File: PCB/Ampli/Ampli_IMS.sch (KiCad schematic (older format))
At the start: 22 parts, among them J1 5227161-3, J2 5227161-3, J3 Conn_01x03_Male, SW1 SS22D0205G2, U1 LT1464CS8, U2 LMP7721

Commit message: modif of schematics
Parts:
- removed U2: LMP7721, Package_SO:SOIC-8_3.9x4.9mm_P1.27mm, symbol Ampli_IMS-rescue:AD8001AR-Amplifier_Operational
- added U?: ADA4625-1, Package_DIP:DIP-8_W7.62mm, symbol Amplifier_Operational:ADA4625-1
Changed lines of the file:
@@
-$EndComp
-$Comp
-L Ampli_IMS-rescue:AD8001AR-Amplifier_Operational U2
-U 1 1 5E63EDD1
-P 4200 4250
-F 0 "U2" H 4544 4296 50  0000 L CNN
-F 1 "LMP7721" H 4544 4205 50  0000 L CNN
-F 2 "Package_SO:SOIC-8_3.9x4.9mm_P1.27mm" H 4100 4050 50  0001 L CNN
-F 3 "https://www.analog.com/media/en/technical-documentation/data-sheets/ad8001.pdf" H 4350 4400 50  0001 C CNN
-	1    4200 4250
-	1    0    0    -1
 $EndComp
 $Comp
@@
 Text Notes 3550 5100 0    50   ~ 0
 Capacités de découplage\n
+$Comp
+L Amplifier_Operational:ADA4625-1 U?
+U 1 1 5E61DA9C
+P 4200 4250
+F 0 "U?" H 4544 4296 50  0000 L CNN
+F 1 "ADA4625-1" H 4544 4205 50  0000 L CNN
+F 2 "Package_DIP:DIP-8_W7.62mm" H 4100 4050 50  0001 L CNN
+F 3 "http://ww1.microchip.com/downloads/en/DeviceDoc/21314g.pdf" H 4350 4400 50  0001 C CNN
+	1    4200 4250
+	1    0    0    -1
+$EndComp
 $EndSCHEMATC

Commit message: tracks realised
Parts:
- U1: renamed from U?; footprint Package_DIP:DIP-8_W7.62mm -> Package_SO:SO-8_3.9x4.9mm_P1.27mm
- U2: renamed from U1; footprint Package_SO:SOIC-8_3.9x4.9mm_P1.27mm -> Package_SO:SO-8_3.9x4.9mm_P1.27mm
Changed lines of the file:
@@
 -15V
 $Comp
-L Ampli_IMS-rescue:Opamp_Dual_Generic-Device U1
+L Ampli_IMS-rescue:Opamp_Dual_Generic-Device U2
 U 1 1 5E681D04
 P 6750 2950
-F 0 "U1" H 6750 3317 50  0000 C CNN
+F 0 "U2" H 6750 3317 50  0000 C CNN
 F 1 "LT1464CS8" H 6750 3226 50  0000 C CNN
-F 2 "Package_SO:SOIC-8_3.9x4.9mm_P1.27mm" H 6750 2950 50  0001 C CNN
+F 2 "Package_SO:SO-8_3.9x4.9mm_P1.27mm" H 6750 2950 50  0001 C CNN
 F 3 "~" H 6750 2950 50  0001 C CNN
 	1    6750 2950
@@
 $EndComp
 $Comp
-L Ampli_IMS-rescue:Opamp_Dual_Generic-Device U1
+L Ampli_IMS-rescue:Opamp_Dual_Generic-Device U2
 U 2 1 5E6829BD
 P 6800 5050
-F 0 "U1" H 6800 5417 50  0000 C CNN
+F 0 "U2" H 6800 5417 50  0000 C CNN
 F 1 "LT1464CS8" H 6800 5326 50  0000 C CNN
-F 2 "Package_SO:SOIC-8_3.9x4.9mm_P1.27mm" H 6800 5050 50  0001 C CNN
+F 2 "Package_SO:SO-8_3.9x4.9mm_P1.27mm" H 6800 5050 50  0001 C CNN
 F 3 "~" H 6800 5050 50  0001 C CNN
 	2    6800 5050
@@
 $EndComp
 $Comp
-L Ampli_IMS-rescue:Opamp_Dual_Generic-Device U1
+L Ampli_IMS-rescue:Opamp_Dual_Generic-Device U2
 U 3 1 5E68341E
 P 1750 6800
-F 0 "U1" H 1708 6846 50  0000 L CNN
+F 0 "U2" H 1708 6846 50  0000 L CNN
 F 1 "LT1464CS8" H 1708 6755 50  0000 L CNN
-F 2 "Package_SO:SOIC-8_3.9x4.9mm_P1.27mm" H 1750 6800 50  0001 C CNN
+F 2 "Package_SO:SO-8_3.9x4.9mm_P1.27mm" H 1750 6800 50  0001 C CNN
 F 3 "~" H 1750 6800 50  0001 C CNN
 	3    1750 6800
@@
 Capacités de découplage\n
 $Comp
-L Amplifier_Operational:ADA4625-1 U?
+L Amplifier_Operational:ADA4625-1 U1
 U 1 1 5E61DA9C
 P 4200 4250
-F 0 "U?" H 4544 4296 50  0000 L CNN
+F 0 "U1" H 4544 4296 50  0000 L CNN
 F 1 "ADA4625-1" H 4544 4205 50  0000 L CNN
-F 2 "Package_DIP:DIP-8_W7.62mm" H 4100 4050 50  0001 L CNN
+F 2 "Package_SO:SO-8_3.9x4.9mm_P1.27mm" H 4100 4050 50  0001 L CNN
 F 3 "http://ww1.microchip.com/downloads/en/DeviceDoc/21314g.pdf" H 4350 4400 50  0001 C CNN
 	1    4200 4250

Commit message: Low noise smd amp
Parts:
- removed R2: 10K MF 1/4W, Resistor_THT:R_Axial_DIN0204_L3.6mm_D1.6mm_P5.08mm_Horizontal, symbol Ampli_IMS-rescue:R-Device
- removed R7: 6.65K MF 1/2W, Resistor_THT:R_Axial_DIN0204_L3.6mm_D1.6mm_P5.08mm_Horizontal, symbol Ampli_IMS-rescue:R-Device
- removed U1: ADA4625-1, Package_SO:SO-8_3.9x4.9mm_P1.27mm, symbol Amplifier_Operational:ADA4625-1
- added U1: LMC6081, Package_SO:SO-8_3.9x4.9mm_P1.27mm, symbol Amplifier_Operational:LMC6081
- C3: renamed from C2; footprint Capacitor_THT:C_Disc_D3.8mm_W2.6mm_P2.50mm -> Capacitor_SMD:C_0805_2012Metric
- C4: renamed from C6; footprint Capacitor_THT:C_Disc_D3.8mm_W2.6mm_P2.50mm -> Capacitor_SMD:C_0805_2012Metric
- C5: renamed from C3; footprint Capacitor_THT:C_Disc_D3.8mm_W2.6mm_P2.50mm -> Capacitor_SMD:C_0805_2012Metric
- C6: renamed from C7; footprint Capacitor_THT:C_Disc_D3.8mm_W2.6mm_P2.50mm -> Capacitor_SMD:C_0805_2012Metric
- C7: renamed from C5; value C_Small -> 100pF; footprint Capacitor_THT:C_Disc_D3.8mm_W2.6mm_P2.50mm -> Capacitor_SMD:C_0805_2012Metric
- J2: renamed from J1; footprint Connector_Coaxial:BNC_Amphenol_B6252HB-NPP3G-50_Horizontal -> Connector_Coaxial:SMA_Amphenol_132203-12_Horizontal
- R1: renamed from R3; footprint Resistor_THT:R_Axial_DIN0204_L3.6mm_D1.6mm_P5.08mm_Horizontal -> Capacitor_SMD:C_0805_2012Metric
- R2: renamed from R1; footprint Resistor_THT:R_Axial_DIN0204_L3.6mm_D1.6mm_P5.08mm_Horizontal -> Capacitor_SMD:C_0805_2012Metric
- R3: renamed from R4; footprint Resistor_THT:R_Axial_DIN0204_L3.6mm_D1.6mm_P5.08mm_Horizontal -> Capacitor_SMD:C_0805_2012Metric
- R4: renamed from R6; value 1.13K MF 1/4W -> 1K; footprint Resistor_THT:R_Axial_DIN0204_L3.6mm_D1.6mm_P5.08mm_Horizontal -> Capacitor_SMD:C_0805_2012Metric
- R5: footprint Resistor_THT:R_Axial_DIN0204_L3.6mm_D1.6mm_P5.08mm_Horizontal -> Capacitor_SMD:C_0805_2012Metric
- renumbered C4 to C2, J3 to J1, J2 to J3
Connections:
- net labels added: +5V, -5V
- net labels removed: +15V, -15V
- wire segments 80 -> 75
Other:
- moved on the sheet: C7, J2, R1, R4

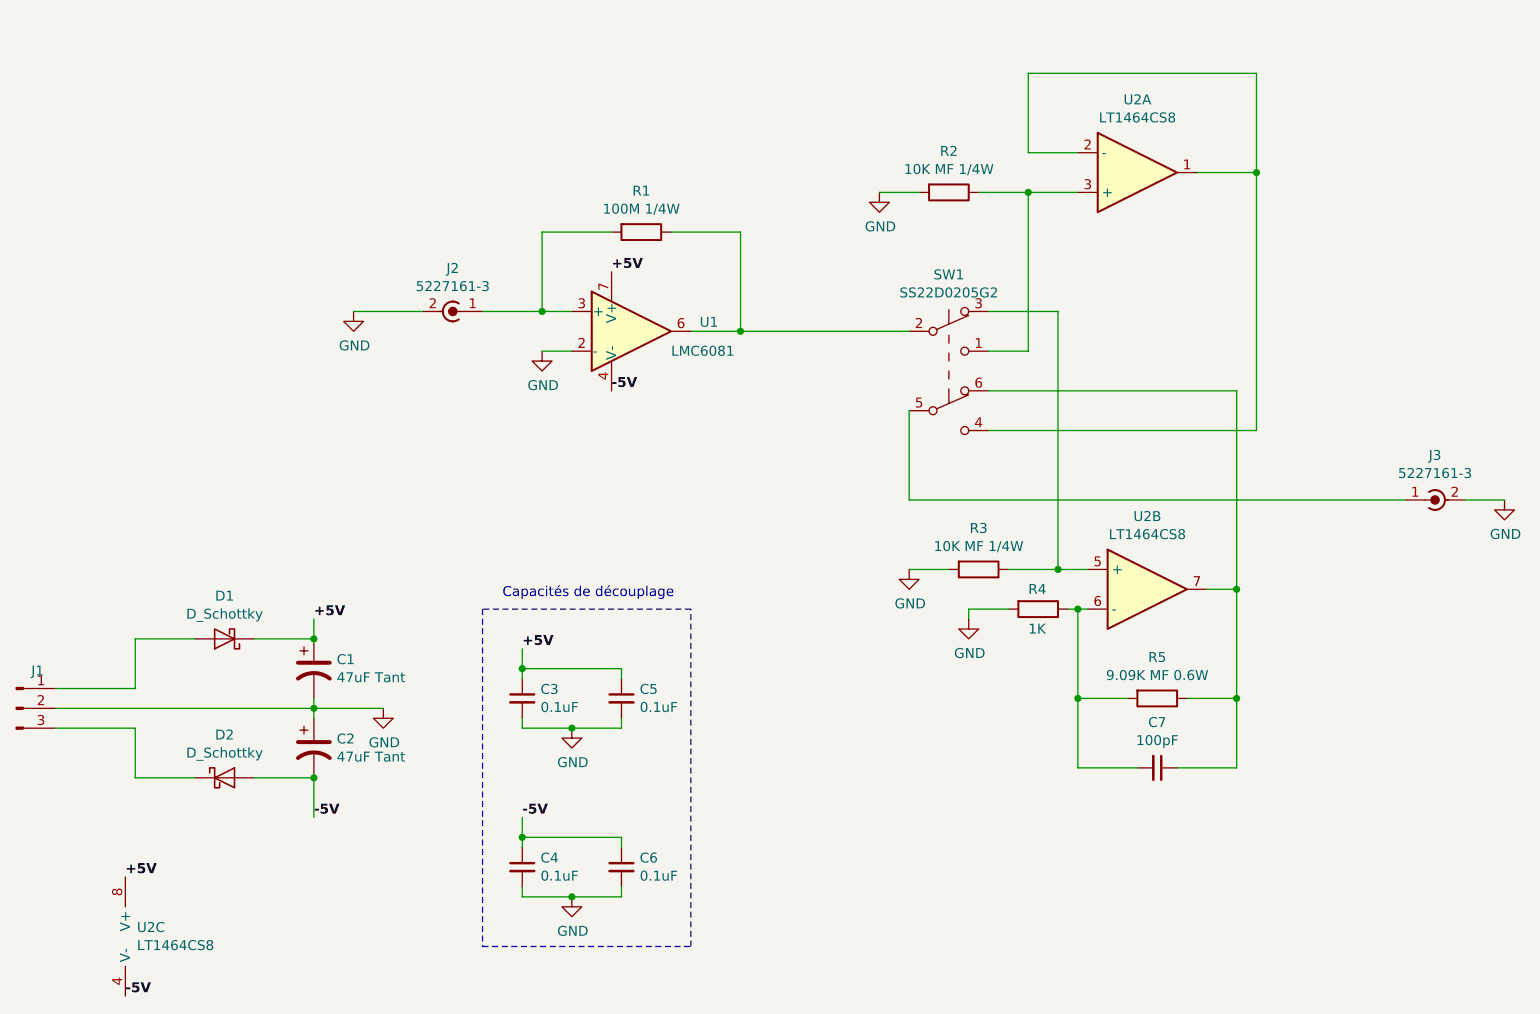
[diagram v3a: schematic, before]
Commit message: SMD + low noise design
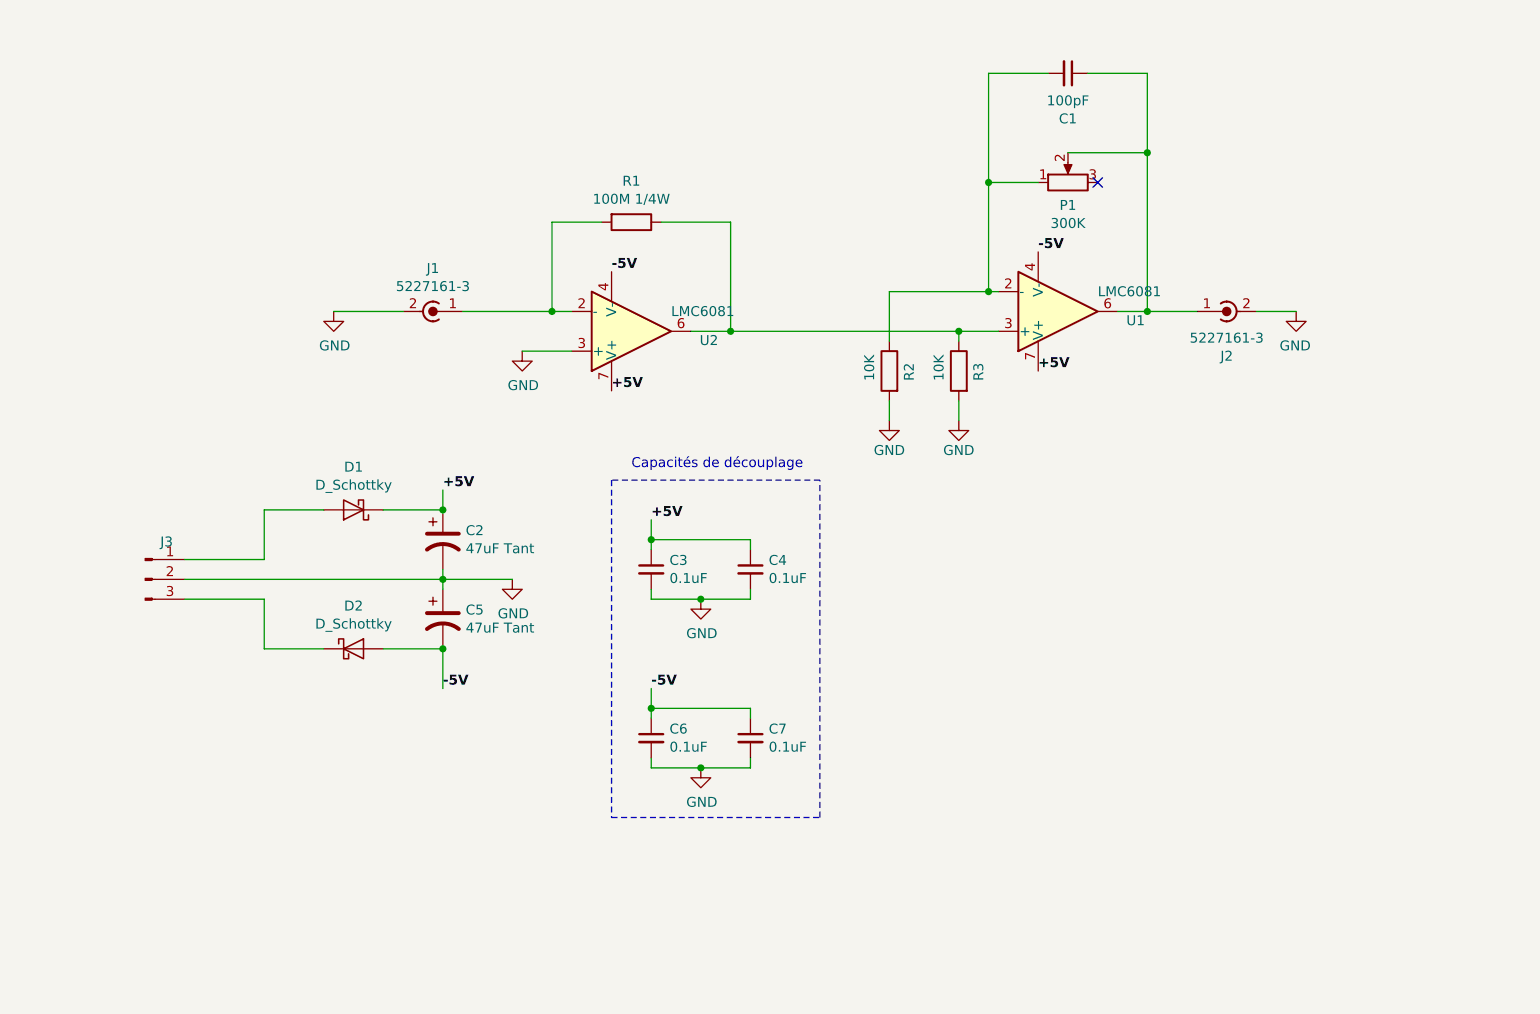
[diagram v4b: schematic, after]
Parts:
- removed R2: 10K MF 1/4W, Capacitor_SMD:C_0805_2012Metric, symbol Ampli_IMS-rescue:R-Device
- removed R5: 9.09K MF 0.6W, Capacitor_SMD:C_0805_2012Metric, symbol Ampli_IMS-rescue:R-Device
- removed SW1: SS22D0205G2, Button_Switch_THT:SW_CuK_JS202011CQN_DPDT_Straight, symbol Ampli_IMS-rescue:SW_Push_DPDT-Switch
- removed U2: LT1464CS8, Package_SO:SO-8_3.9x4.9mm_P1.27mm, symbol Ampli_IMS-rescue:Opamp_Dual_Generic-Device
- added P1: 300K, Potentiometer_THT:Potentiometer_Alps_RK09Y11_Single_Horizontal, symbol Device:R_POT
- added U1: LMC6081, Package_SO:SO-8_3.9x4.9mm_P1.27mm, symbol Amplifier_Operational:LMC6081
- R2: renamed from R4; value 1K -> 10K
- R3: value 10K MF 1/4W -> 10K
- renumbered C7 to C1, C1 to C2, C5 to C4, C2 to C5, C4 to C6, C6 to C7, J2 to J1, J3 to J2, J1 to J3, U1 to U2
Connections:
- net +5V: now also U1.7 (V+)
- net -5V: now also U1.4 (V-)
- net GND: now also U2.3 (+); no longer U2.2 (-)
- net at C1.1: now also J2.1 (In), P1.2, U1.6
- net at C1.2, R2.1: now also P1.1, U1.2 (-)
- net at R1.1, U2.6: now also R3.1, U1.3 (+)
- net at J1.1 (In), R1.2: now also U2.2 (-); no longer U2.3 (+)
- no-connect marks 0 -> 1
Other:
- moved on the sheet: C1, C2, C3, C4, C5, C6, C7, D1, D2, J1, J2, J3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

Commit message: Small mistakes
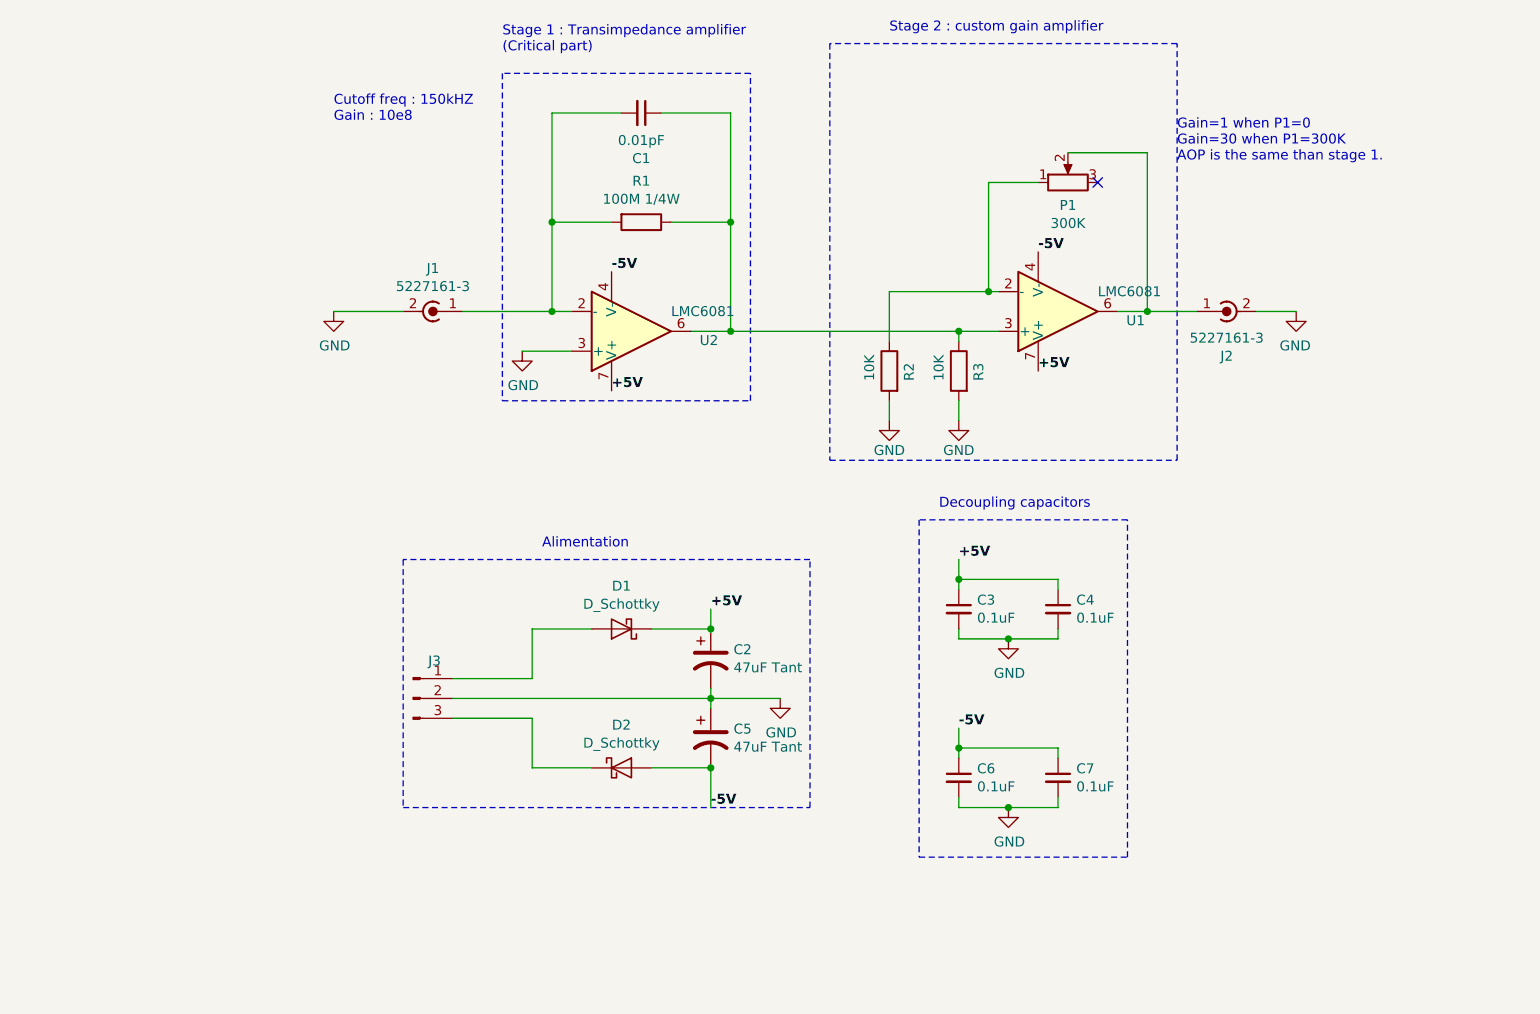
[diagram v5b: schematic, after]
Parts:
- C1: value 100pF -> 0.01pF
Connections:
- net at J2.1 (In), P1.2, U1.6: no longer C1.1
- net at P1.1, R2.1, U1.2 (-): no longer C1.2
- net at J1.1 (In), R1.2, U2.2 (-): now also C1.2
- net at R1.1, R3.1, U1.3 (+)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: now also C1.1
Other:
- note added: "Alimentation\n"
- note added: "Cutoff freq : 150kHZ\nGain : 10e8"
- note added: "Decoupling capacitors"
- note added: "Gain=1 when P1=0\nGain=30 when P1=300K\nAOP is the same than stage 1."
- note added: "Stage 1 : Transimpedance amplifier\n(Critical part)"
- note added: "Stage 2 : custom gain amplifier"
- note removed: "Capacités de découplage\n"
- moved on the sheet: C1, C2, C3, C4, C5, C6, C7, D1, D2, J3, R1

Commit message: GND guards are neat!
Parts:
- removed C4, C7: 0.1uF, Capacitor_SMD:C_0805_2012Metric, symbol Ampli_IMS-rescue:C_Small-Device
- removed U1, U2: LMC6081, Package_SO:SO-8_3.9x4.9mm_P1.27mm, symbol Amplifier_Operational:LMC6081
- added U1: LMC6082, Package_SO:SO-8_3.9x4.9mm_P1.27mm, symbol Amplifier_Operational:LMC6082
- renumbered C3 to C2, C2 to C3, C5 to C4, C6 to C5
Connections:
- net +5V: now also U1.8 (V+)
- net -5V: now also U1.4 (V-)
- net GND: now also U1.3 (+)
- net at C1.1, R1.1, R3.1: now also U1.1, U1.5 (+)
- net at C1.2, J1.1 (In), R1.2: now also U1.2 (-)
- net at J2.1 (In), P1.2: now also P1.3, U1.7
- net at P1.1, R2.1: now also U1.6 (-)
- no-connect marks 1 -> 0
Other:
- note removed: "Stage 1 : Transimpedance amplifier\n(Critical part)"
- note removed: "Stage 2 : custom gain amplifier"

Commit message: Improve PCBs
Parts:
- C3, C4: footprint Capacitor_THT:CP_Radial_Tantal_D5.0mm_P5.00mm -> Capacitor_Tantalum_SMD:CP_EIA-3216-18_Kemet-A_Pad1.58x1.35mm_HandSolder
- D1, D2: footprint Diode_THT:D_5W_P10.16mm_Horizontal -> Diode_SMD:D_0805_2012Metric_Castellated
- R1: value 100M 1/4W -> 100M
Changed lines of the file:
@@
 F 0 "C4" H 4715 5846 50  0000 L CNN
 F 1 "47uF Tant" H 4715 5755 50  0000 L CNN
-F 2 "Capacitor_THT:CP_Radial_Tantal_D5.0mm_P5.00mm" H 4600 5800 50  0001 C CNN
+F 2 "Capacitor_Tantalum_SMD:CP_EIA-3216-18_Kemet-A_Pad1.58x1.35mm_HandSolder" H 4600 5800 50  0001 C CNN
 F 3 "~" H 4600 5800 50  0001 C CNN
 	1    4600 5800
@@
 F 0 "C3" H 4715 5446 50  0000 L CNN
 F 1 "47uF Tant" H 4715 5355 50  0000 L CNN
-F 2 "Capacitor_THT:CP_Radial_Tantal_D5.0mm_P5.00mm" H 4600 5400 50  0001 C CNN
+F 2 "Capacitor_Tantalum_SMD:CP_EIA-3216-18_Kemet-A_Pad1.58x1.35mm_HandSolder" H 4600 5400 50  0001 C CNN
 F 3 "~" H 4600 5400 50  0001 C CNN
 	1    4600 5400
@@
 P 4250 3200
 F 0 "R1" V 4043 3200 50  0000 C CNN
-F 1 "100M 1/4W" V 4134 3200 50  0000 C CNN
+F 1 "100M" V 4134 3200 50  0000 C CNN
 F 2 "Capacitor_SMD:C_0805_2012Metric" V 4180 3200 50  0001 C CNN
 F 3 "~" H 4250 3200 50  0001 C CNN
@@
 F 0 "D1" H 4150 5034 50  0000 C CNN
 F 1 "D_Schottky" H 4150 5125 50  0000 C CNN
-F 2 "Diode_THT:D_5W_P10.16mm_Horizontal" H 4150 5250 50  0001 C CNN
+F 2 "Diode_SMD:D_0805_2012Metric_Castellated" H 4150 5250 50  0001 C CNN
 F 3 "~" H 4150 5250 50  0001 C CNN
 	1    4150 5250
@@
 F 0 "D2" H 4150 6166 50  0000 C CNN
 F 1 "D_Schottky" H 4150 6075 50  0000 C CNN
-F 2 "Diode_THT:D_5W_P10.16mm_Horizontal" H 4150 5950 50  0001 C CNN
+F 2 "Diode_SMD:D_0805_2012Metric_Castellated" H 4150 5950 50  0001 C CNN
 F 3 "~" H 4150 5950 50  0001 C CNN
 	1    4150 5950
@@
 -5V
 Wire Wire Line
-	5850 6150 6100 6150
-Wire Wire Line
 	5850 6100 5850 6150
 $Comp
 L Ampli_IMS-rescue:GND-power #PWR08
 U 1 1 5E67E967
-P 6100 6150
-F 0 "#PWR08" H 6100 5900 50  0001 C CNN
-F 1 "GND" H 6105 5977 50  0000 C CNN
-F 2 "" H 6100 6150 50  0001 C CNN
-F 3 "" H 6100 6150 50  0001 C CNN
-	1    6100 6150
+P 5850 6150
+F 0 "#PWR08" H 5850 5900 50  0001 C CNN
+F 1 "GND" H 5855 5977 50  0000 C CNN
+F 2 "" H 5850 6150 50  0001 C CNN
+F 3 "" H 5850 6150 50  0001 C CNN
+	1    5850 6150
 	1    0    0    -1
 $EndComp
@@
 L Ampli_IMS-rescue:GND-power #PWR06
 U 1 1 5E67CE1A
-P 6100 5300
-F 0 "#PWR06" H 6100 5050 50  0001 C CNN
-F 1 "GND" H 6105 5127 50  0000 C CNN
-F 2 "" H 6100 5300 50  0001 C CNN
-F 3 "" H 6100 5300 50  0001 C CNN
-	1    6100 5300
-	1    0    0    -1
-$EndComp
-Wire Wire Line
-	5850 5250 5850 5300
-Wire Wire Line
-	5850 5300 6100 5300
+P 5850 5350
+F 0 "#PWR06" H 5850 5100 50  0001 C CNN
+F 1 "GND" H 5855 5177 50  0000 C CNN
+F 2 "" H 5850 5350 50  0001 C CNN
+F 3 "" H 5850 5350 50  0001 C CNN
+	1    5850 5350
+	1    0    0    -1
+$EndComp
 Text Label 5850 4900 0    50   ~ 10
 +5V
@@
 	-1   0    0    -1
 $EndComp
+Wire Wire Line
+	5850 5250 5850 5350
 $EndSCHEMATC
